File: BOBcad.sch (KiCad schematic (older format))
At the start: 26 parts, among them J1 CN3791, J10 Programming, J12 EN, J2 JTAG, J3 DS18B20, J4 BME280, J6 Load Cell, J7 DS3231, Q1 S8050, Q2 S8050, U1 NCP380, U2 HX711, U3 WIPY, U4 ESP32_DevKit_V1

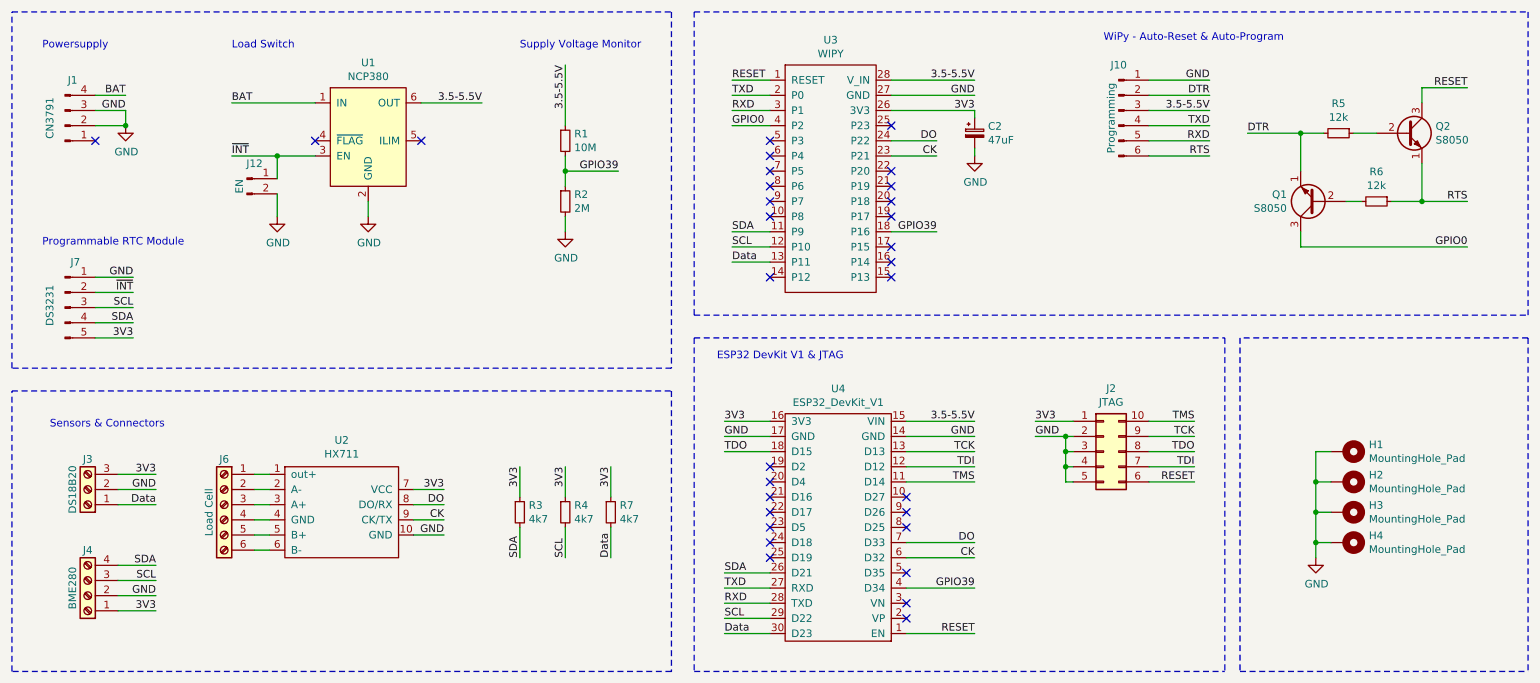
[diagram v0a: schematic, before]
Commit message: v1.0.2
Added solar voltage monitoring
Modified power plane
Added two more capacitors for 3v3 lines to sensors
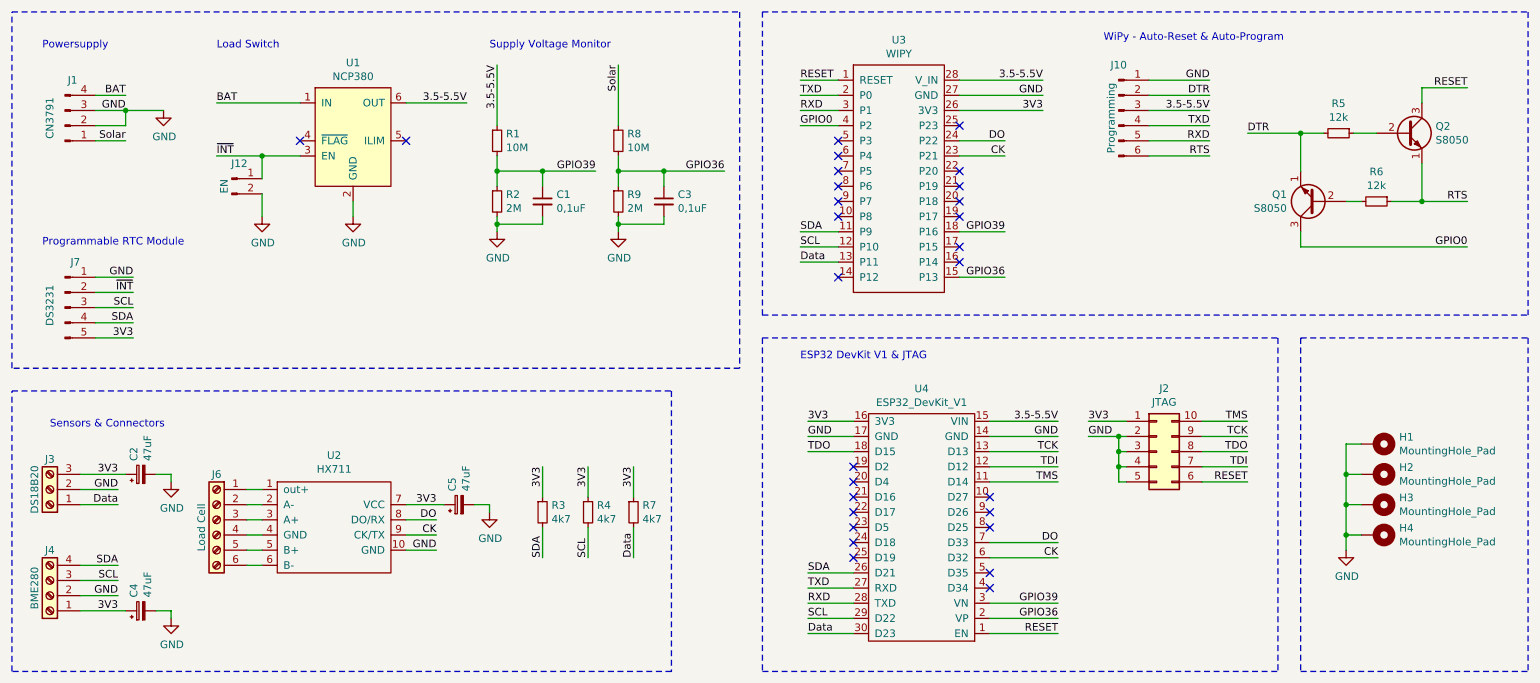
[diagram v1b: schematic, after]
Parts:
- added C1, C3: 0,1uF, Capacitors_SMD:C_0805_HandSoldering, symbol Device:C_Small
- added C4, C5: 47uF, Capacitors_ThroughHole:CP_Radial_D4.0mm_P1.50mm, symbol Device:CP_Small
- added R8: 10M, Resistors_SMD:R_0805_HandSoldering, symbol Device:R_Small
- added R9: 2M, Resistors_SMD:R_0805_HandSoldering, symbol Device:R_Small
- Q1, Q2: Config Fit -> pycom
- R1: Description RES 10M OHM 1% 1/4W 1206 -> RES SMD 10M OHM 1% 1/8W 0805; MFG P/N RMCF1206FT10M0CT-ND -> 311-10.0MCRCT-ND; Part Link https://www.digikey.ch/short/4300cq -> https://www.digikey.ch/short/cmw0fhc7
- R2: Description RES SMD 2M OHM 1% 1/4W 1206 -> RES SMD 2M OHM 1% 1/8W 0805; MFG P/N YAG3858CT-ND -> 311-2.00MCRCT-ND; Part Link https://www.digikey.ch/short/430077 -> https://www.digikey.ch/short/03pbtm30
- R3, R4, R7: Description RES SMD 4.7K OHM 1% 1/4W 1206 -> RES SMD 4.7K OHM 1% 1/8W 0805; MFG P/N YAG3884CT-ND -> 311-4.70KCRCT-ND; Part Link https://www.digikey.ch/short/4300pt -> https://www.digikey.ch/short/twprbz44
- R5, R6: Config (none) -> pycom; Description (none) -> RES SMD 12K OHM 1% 1/8W 0805; MFG P/N (none) -> 311-12.0KCRCT-ND; Part Link (none) -> https://www.digikey.ch/short/mn4dm8dn
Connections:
- net 3V3: now also C4.1, C5.1
- net GND: now also C1.2, C3.2, C4.2, C5.2, R9.2
- net GPIO39: now also U4.3 (VN), C1.1; no longer U4.4 (D34)
- net GPIO36: now reaches U3.15 (P13)
- net GPIO36: now also U4.2 (VP), C3.1, R8.2, R9.1
- net Solar: now reaches J1.1 (Pin_1)
- net Solar: now also R8.1
- no-connect marks 31 -> 28
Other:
- moved on the sheet: H1, H2, H3, H4, J12, J2, J3, J4, J6, R1, R2, R3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
